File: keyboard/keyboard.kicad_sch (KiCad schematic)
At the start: 131 parts, among them SW1 MX_SW_HS, SW10 MX_SW_HS, SW11 MX_SW_HS, SW12 MX_SW_HS, SW13 MX_SW_HS, SW14 MX_SW_HS, SW15 MX_SW_HS, SW16 MX_SW_HS, SW17 MX_SW_HS, SW18 MX_SW_HS, SW19 MX_SW_HS, SW2 MX_SW_HS, SW20 MX_SW_HS, SW21 MX_SW_HS, SW22 MX_SW_HS, SW23 MX_SW_HS, SW24 MX_SW_HS, SW25 MX_SW_HS, SW26 MX_SW_HS, SW27 MX_SW_HS, SW28 MX_SW_HS, SW29 MX_SW_HS, SW3 MX_SW_HS, SW30 MX_SW_HS, SW31 MX_SW_HS, SW32 MX_SW_HS, SW33 MX_SW_HS, SW34 MX_SW_HS, SW35 MX_SW_HS, SW36 MX_SW_HS, SW37 MX_SW_HS, SW38 MX_SW_HS, SW39 MX_SW_HS, SW4 MX_SW_HS, SW40 MX_SW_HS, SW41 MX_SW_HS, SW42 MX_SW_HS, SW43 MX_SW_HS, SW44 MX_SW_HS, SW45 MX_SW_HS, SW46 MX_SW_HS, SW47 MX_SW_HS, SW48 MX_SW_HS, SW49 MX_SW_HS, SW5 MX_SW_HS, SW50 MX_SW_HS, SW51 MX_SW_HS, SW52 MX_SW_HS, SW53 MX_SW_HS, SW54 MX_SW_HS, SW55 MX_SW_HS, SW56 MX_SW_HS, SW57 MX_SW_HS, SW58 MX_SW_HS, SW59 MX_SW_HS, SW6 MX_SW_HS, SW60 MX_SW_HS, SW61 MX_SW_HS, SW62 MX_SW_HS, SW63 MX_SW_HS, SW64 MX_SW_HS, SW7 MX_SW_HS, SW8 MX_SW_HS, SW9 MX_SW_HS, U1 ProMicro

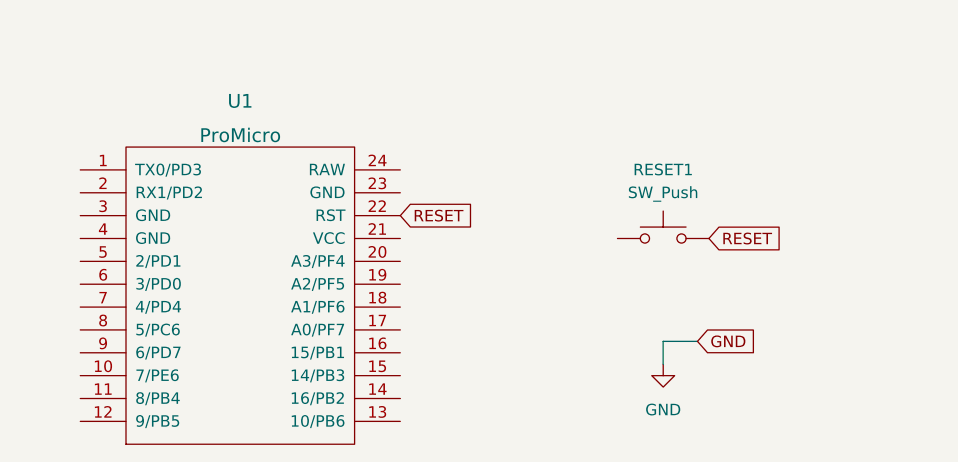
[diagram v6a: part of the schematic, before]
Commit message: Start to add the wiring for the keyboard
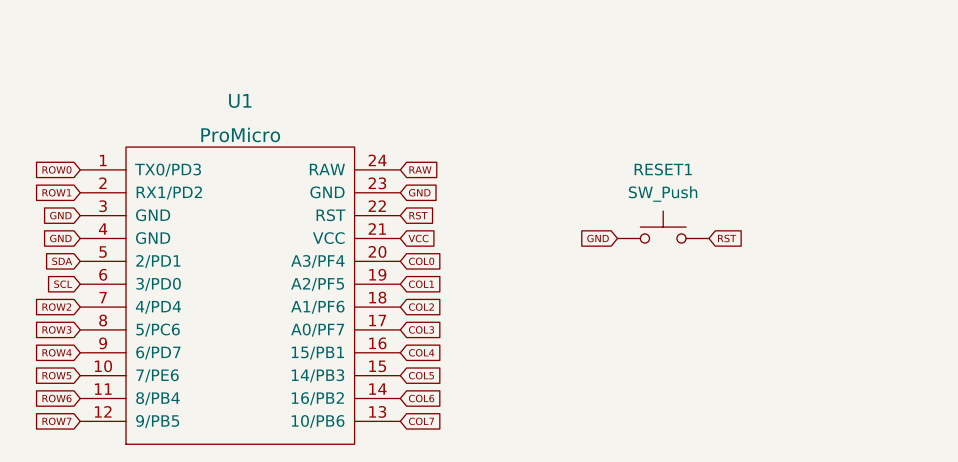
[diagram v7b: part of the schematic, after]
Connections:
- net COL0: now also U1.20 (A3/PF4)
- net COL1: now also U1.19 (A2/PF5)
- net COL2: now also U1.18 (A1/PF6)
- net COL3: now also U1.17 (A0/PF7)
- net COL4: now also U1.16 (15/PB1)
- net COL5: now also U1.15 (14/PB3)
- net COL6: now also U1.14 (16/PB2)
- net COL7: now also U1.13 (10/PB6)
- net GND: now also RESET1.1, U1.23 (GND), U1.3 (GND), U1.4 (GND)
- net ROW0: now also U1.1 (TX0/PD3)
- net ROW1: now also U1.2 (RX1/PD2)
- net ROW2: now also U1.7 (4/PD4)
- net ROW3: now also U1.8 (5/PC6)
- net ROW4: now also U1.9 (6/PD7)
- net ROW5: now also U1.10 (7/PE6)
- net ROW6: now also U1.11 (8/PB4)
- net ROW7: now also U1.12 (9/PB5)
- net VCC: now reaches U1.21 (VCC)
- net RAW: now reaches U1.24 (RAW)
- net SDA: now reaches U1.5 (2/PD1)
- net SCL: now reaches U1.6 (3/PD0)
- net RESET renamed RST

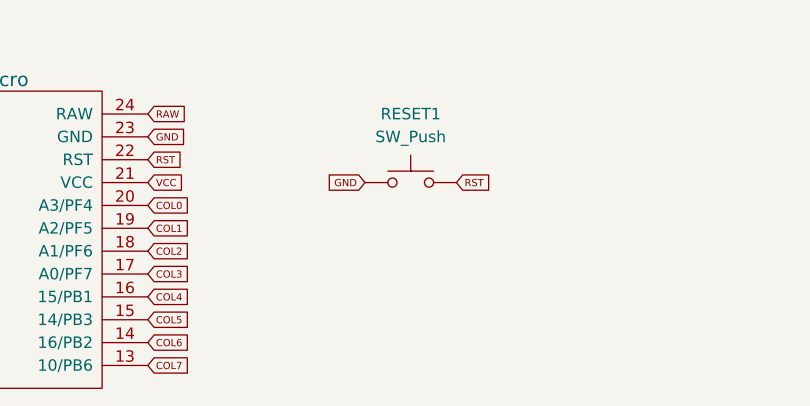
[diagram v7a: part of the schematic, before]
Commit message: Add the power and clean up the reset button a little
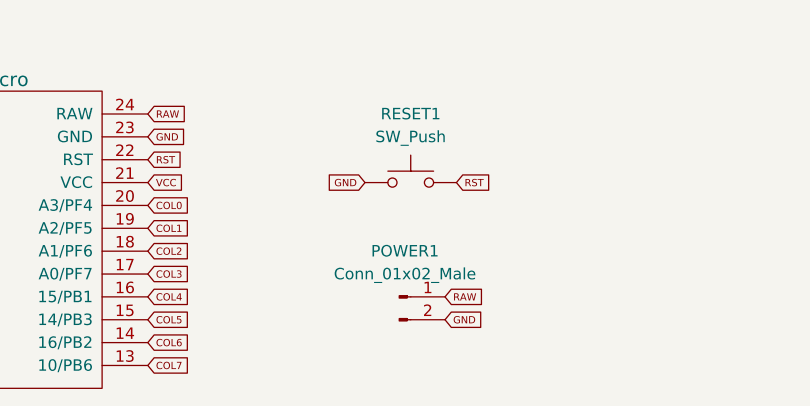
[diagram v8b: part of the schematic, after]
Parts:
- added POWER1: Conn_01x02_Male, symbol Connector:Conn_01x02_Male
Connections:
- net GND: now also POWER1.2 (Pin_2)
- net RAW: now also POWER1.1 (Pin_1)
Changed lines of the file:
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@@
+    )
+  )
+  (global_label "GND" (shape input) (at 100.33 172.72 0) (fields_autoplaced)
+    (effects (font (size 0.8 0.8)) (justify left))
+    (property "Intersheet References" "${INTERSHEET_REFS}" (id 0) (at 104.2881 172.67 0)
+      (effects (font (size 0.8 0.8)) (justify left) hide)
     )
   )
@@
     (property "Intersheet References" "${INTERSHEET_REFS}" (id 0) (at 176.7143 67.2725 0)
       (effects (font (size 0.6 0.6)) (justify right) hide)
+    )
+  )
+  (global_label "RAW" (shape input) (at 100.33 170.18 0) (fields_autoplaced)
+    (effects (font (size 0.8 0.8)) (justify left))
+    (property "Intersheet References" "${INTERSHEET_REFS}" (id 0) (at 104.25 170.13 0)
+      (effects (font (size 0.8 0.8)) (justify left) hide)
     )
   )
@@
     )
     (property "Datasheet" "~" (id 3) (at 107.95 68.58 0)
+      (effects (font (size 1.27 1.27)) hide)
+    )
+    (pin "1")
+    (pin "2")
+  )
+  (symbol (lib_id "Connector:Conn_01x02_Male") (at 95.25 170.18 0) (unit 1)
+    (in_bom yes) (on_board yes) (fields_autoplaced)
+    (property "Reference" "POWER1" (id 0) (at 95.885 165.1 0))
+    (property "Value" "Conn_01x02_Male" (id 1) (at 95.885 167.64 0))
+    (property "Footprint" "" (id 2) (at 95.25 170.18 0)
+      (effects (font (size 1.27 1.27)) hide)
+    )
+    (property "Datasheet" "~" (id 3) (at 95.25 170.18 0)
       (effects (font (size 1.27 1.27)) hide)
     )
@@
       (reference "D64") (unit 1) (value "1N4148") (footprint "Diode_THT:D_DO-35_SOD27_P7.62mm_Horizontal")
     )
+    (path "/0ea7d412-6277-4227-b71e-6e4e29ffda6b"
+      (reference "POWER1") (unit 1) (value "Conn_01x02_Male") (footprint "Connector_PinHeader_2.54mm:PinHeader_1x02_P2.54mm_Vertical")
+    )
     (path "/69aaefbf-88d4-415d-ad96-2a6ff3ee3a2f"
